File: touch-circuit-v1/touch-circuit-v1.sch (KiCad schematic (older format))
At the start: 11 parts, among them U1 Opamp_Dual_Generic

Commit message: add footprints
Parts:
- BT1: footprint (none) -> Battery:BatteryHolder_LINX_BAT-HLD-012-SMT
- C1: footprint (none) -> Capacitor_SMD:C_0805_2012Metric_Pad1.15x1.40mm_HandSolder
- D1: footprint (none) -> Diode_SMD:D_0805_2012Metric_Pad1.15x1.40mm_HandSolder
- D2: footprint (none) -> LED_SMD:LED_0805_2012Metric_Pad1.15x1.40mm_HandSolder
- R1, R2, R3, R4, R5, R6: footprint (none) -> Resistor_SMD:R_0805_2012Metric_Pad1.15x1.40mm_HandSolder
- U1: footprint (none) -> Package_SO:SO-8_5.3x6.2mm_P1.27mm
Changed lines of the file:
@@
 F 0 "U1" H 7050 4117 50  0000 C CNN
 F 1 "Opamp_Dual_Generic" H 7050 4026 50  0000 C CNN
-F 2 "" H 7050 3750 50  0001 C CNN
+F 2 "Package_SO:SO-8_5.3x6.2mm_P1.27mm" H 7050 3750 50  0001 C CNN
 F 3 "~" H 7050 3750 50  0001 C CNN
 	2    7050 3750
@@
 F 0 "U1" H 3008 3396 50  0000 L CNN
 F 1 "Opamp_Dual_Generic" H 3008 3305 50  0000 L CNN
-F 2 "" H 3050 3350 50  0001 C CNN
+F 2 "Package_SO:SO-8_5.3x6.2mm_P1.27mm" H 3050 3350 50  0001 C CNN
 F 3 "~" H 3050 3350 50  0001 C CNN
 	3    3050 3350
@@
 F 0 "U1" H 5200 3517 50  0000 C CNN
 F 1 "Opamp_Dual_Generic" H 5200 3426 50  0000 C CNN
-F 2 "" H 5200 3150 50  0001 C CNN
+F 2 "Package_SO:SO-8_5.3x6.2mm_P1.27mm" H 5200 3150 50  0001 C CNN
 F 3 "~" H 5200 3150 50  0001 C CNN
 	1    5200 3150
@@
 F 0 "D2" H 7892 3495 50  0000 C CNN
 F 1 "LED" H 7892 3586 50  0000 C CNN
-F 2 "" H 7900 3750 50  0001 C CNN
+F 2 "LED_SMD:LED_0805_2012Metric_Pad1.15x1.40mm_HandSolder" H 7900 3750 50  0001 C CNN
 F 3 "~" H 7900 3750 50  0001 C CNN
 	1    7900 3750
@@
 F 0 "R2" H 4518 2846 50  0000 L CNN
 F 1 "R_US" H 4518 2755 50  0000 L CNN
-F 2 "" V 4490 2790 50  0001 C CNN
+F 2 "Resistor_SMD:R_0805_2012Metric_Pad1.15x1.40mm_HandSolder" V 4490 2790 50  0001 C CNN
 F 3 "~" H 4450 2800 50  0001 C CNN
 	1    4450 2800
@@
 F 0 "C1" H 6415 3946 50  0000 L CNN
 F 1 "C" H 6415 3855 50  0000 L CNN
-F 2 "" H 6338 3750 50  0001 C CNN
+F 2 "Capacitor_SMD:C_0805_2012Metric_Pad1.15x1.40mm_HandSolder" H 6338 3750 50  0001 C CNN
 F 3 "~" H 6300 3900 50  0001 C CNN
 	1    6300 3900
@@
 F 0 "D1" H 6050 2934 50  0000 C CNN
 F 1 "D" H 6050 3025 50  0000 C CNN
-F 2 "" H 6050 3150 50  0001 C CNN
+F 2 "Diode_SMD:D_0805_2012Metric_Pad1.15x1.40mm_HandSolder" H 6050 3150 50  0001 C CNN
 F 3 "~" H 6050 3150 50  0001 C CNN
 	1    6050 3150
@@
 F 0 "R3" H 4518 3546 50  0000 L CNN
 F 1 "R_US" H 4518 3455 50  0000 L CNN
-F 2 "" V 4490 3490 50  0001 C CNN
+F 2 "Resistor_SMD:R_0805_2012Metric_Pad1.15x1.40mm_HandSolder" V 4490 3490 50  0001 C CNN
 F 3 "~" H 4450 3500 50  0001 C CNN
 	1    4450 3500
@@
 F 0 "R6" H 8218 4046 50  0000 L CNN
 F 1 "R_US" H 8218 3955 50  0000 L CNN
-F 2 "" V 8190 3990 50  0001 C CNN
+F 2 "Resistor_SMD:R_0805_2012Metric_Pad1.15x1.40mm_HandSolder" V 8190 3990 50  0001 C CNN
 F 3 "~" H 8150 4000 50  0001 C CNN
 	1    8150 4000
@@
 F 0 "R4" H 5868 3446 50  0000 L CNN
 F 1 "R_US" H 5868 3355 50  0000 L CNN
-F 2 "" V 5840 3390 50  0001 C CNN
+F 2 "Resistor_SMD:R_0805_2012Metric_Pad1.15x1.40mm_HandSolder" V 5840 3390 50  0001 C CNN
 F 3 "~" H 5800 3400 50  0001 C CNN
 	1    5800 3400
@@
 F 0 "R5" H 6368 3446 50  0000 L CNN
 F 1 "R_US" H 6368 3355 50  0000 L CNN
-F 2 "" V 6340 3390 50  0001 C CNN
+F 2 "Resistor_SMD:R_0805_2012Metric_Pad1.15x1.40mm_HandSolder" V 6340 3390 50  0001 C CNN
 F 3 "~" H 6300 3400 50  0001 C CNN
 	1    6300 3400
@@
 F 0 "R1" H 4068 3546 50  0000 L CNN
 F 1 "R_US" H 4068 3455 50  0000 L CNN
-F 2 "" V 4040 3490 50  0001 C CNN
+F 2 "Resistor_SMD:R_0805_2012Metric_Pad1.15x1.40mm_HandSolder" V 4040 3490 50  0001 C CNN
 F 3 "~" H 4000 3500 50  0001 C CNN
 	1    4000 3500
@@
 F 0 "BT1" H 2268 3496 50  0000 L CNN
 F 1 "Battery_Cell" H 2268 3405 50  0000 L CNN
-F 2 "" V 2150 3460 50  0001 C CNN
+F 2 "Battery:BatteryHolder_LINX_BAT-HLD-012-SMT" V 2150 3460 50  0001 C CNN
 F 3 "~" V 2150 3460 50  0001 C CNN
 	1    2150 3400

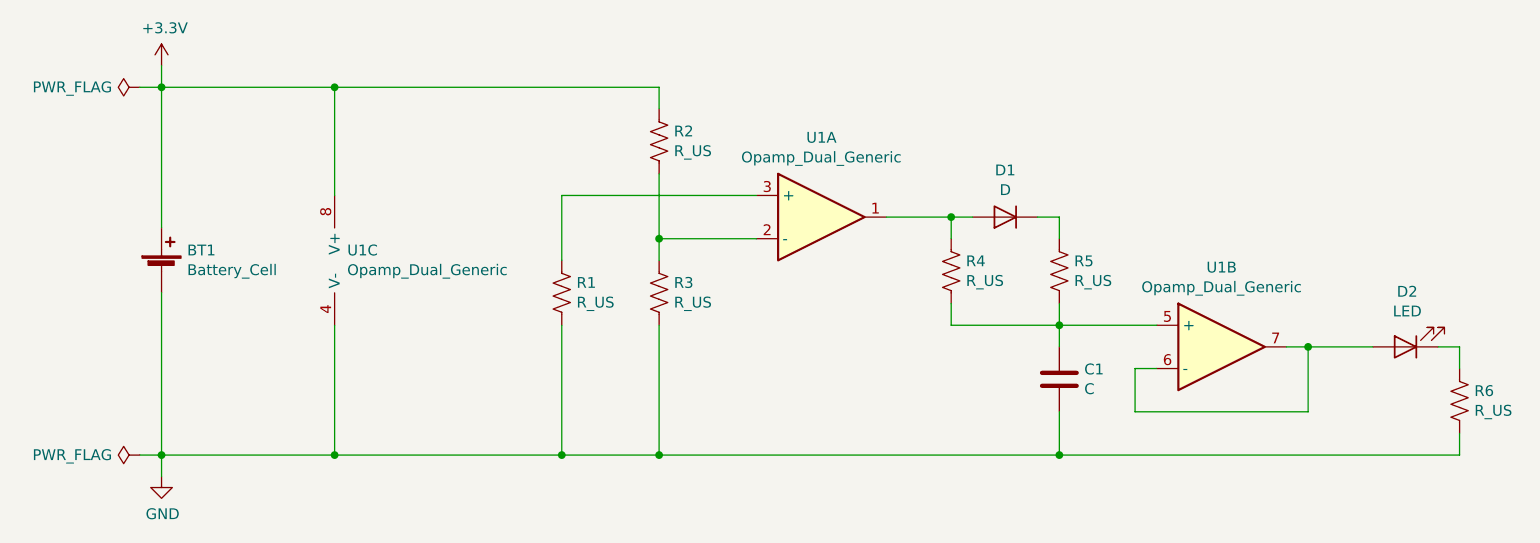
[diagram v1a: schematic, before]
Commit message: add mounting holes
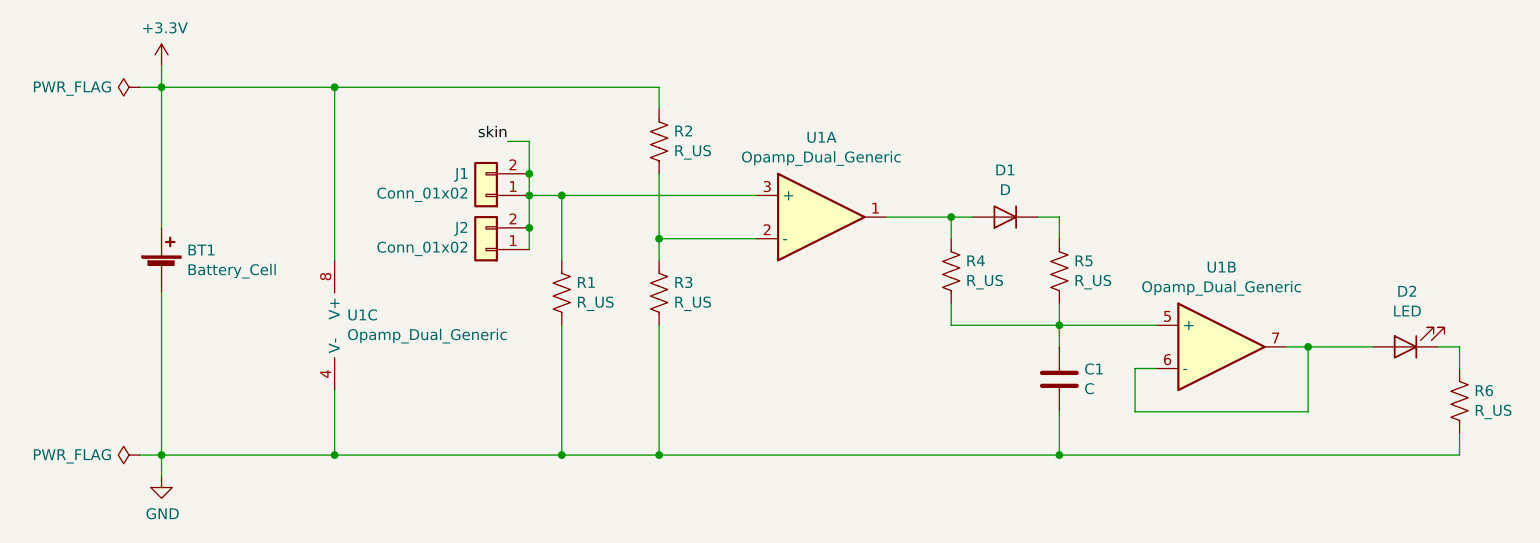
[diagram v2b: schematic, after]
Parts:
- added J1, J2: Conn_01x02, Connector_PinHeader_2.54mm:PinHeader_1x02_P2.54mm_Vertical, symbol Connector_Generic:Conn_01x02
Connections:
- net skin: now reaches R1.1, U1.3 (+)
- net skin: now also J1.1 (Pin_1), J1.2 (Pin_2), J2.1 (Pin_1), J2.2 (Pin_2)
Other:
- moved on the sheet: U1C
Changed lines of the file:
@@
 EESchema Schematic File Version 4
+LIBS:touch-circuit-v1-cache
 EELAYER 26 0
 EELAYER END
@@
 L Device:Opamp_Dual_Generic U1
 U 3 1 5E3073DB
-P 3050 3350
-F 0 "U1" H 3008 3396 50  0000 L CNN
-F 1 "Opamp_Dual_Generic" H 3008 3305 50  0000 L CNN
-F 2 "Package_SO:SO-8_5.3x6.2mm_P1.27mm" H 3050 3350 50  0001 C CNN
-F 3 "~" H 3050 3350 50  0001 C CNN
-	3    3050 3350
+P 3050 3650
+F 0 "U1" H 3008 3696 50  0000 L CNN
+F 1 "Opamp_Dual_Generic" H 3008 3605 50  0000 L CNN
+F 2 "Package_SO:SO-8_5.3x6.2mm_P1.27mm" H 3050 3650 50  0001 C CNN
+F 3 "~" H 3050 3650 50  0001 C CNN
+	3    3050 3650
 	1    0    0    -1
 $EndComp
@@
 Connection ~ 4450 3250
 Wire Wire Line
-	4900 3050 4000 3050
-Wire Wire Line
-	4000 3050 4000 3350
-Wire Wire Line
 	5800 3550 5800 3650
 Wire Wire Line
@@
 Connection ~ 5800 3150
 Wire Wire Line
-	2950 2550 2950 3050
-Wire Wire Line
-	2950 3650 2950 4250
+	2950 2550 2950 3350
+Wire Wire Line
+	2950 3950 2950 4250
 Wire Wire Line
 	2950 4250 4000 4250
@@
 Wire Wire Line
 	2050 4250 2150 4250
+Text Label 3750 2800 2    50   ~ 0
+skin
+$Comp
+L Connector_Generic:Conn_01x02 J1
+U 1 1 5E30C6B3
+P 3650 3050
+F 0 "J1" H 3730 2950 50  0000 L CNN
+F 1 "Conn_01x02" H 3730 3041 50  0000 L CNN
+F 2 "Connector_PinHeader_2.54mm:PinHeader_1x02_P2.54mm_Vertical" H 3650 3050 50  0001 C CNN
+F 3 "~" H 3650 3050 50  0001 C CNN
+	1    3650 3050
+	-1   0    0    1
+$EndComp
+$Comp
+L Connector_Generic:Conn_01x02 J2
+U 1 1 5E312800
+P 3650 3300
+F 0 "J2" H 3730 3200 50  0000 L CNN
+F 1 "Conn_01x02" H 3730 3291 50  0000 L CNN
+F 2 "Connector_PinHeader_2.54mm:PinHeader_1x02_P2.54mm_Vertical" H 3650 3300 50  0001 C CNN
+F 3 "~" H 3650 3300 50  0001 C CNN
+	1    3650 3300
+	-1   0    0    1
+$EndComp
+Wire Wire Line
+	4900 3050 4000 3050
+Wire Wire Line
+	4000 3050 4000 3350
+Connection ~ 3850 3050
+Wire Wire Line
+	3850 3050 3850 2950
+Connection ~ 3850 3200
+Wire Wire Line
+	3850 3200 3850 3050
+Wire Wire Line
+	3850 3200 3850 3300
+Wire Wire Line
+	3750 2800 3850 2800
+Wire Wire Line
+	3850 2800 3850 2950
+Connection ~ 3850 2950
+Wire Wire Line
+	3850 3050 4000 3050
+Connection ~ 4000 3050
 $EndSCHEMATC

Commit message: add silk and update mounting footprints
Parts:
- J1, J2: footprint Connector_PinHeader_2.54mm:PinHeader_1x02_P2.54mm_Vertical -> touch-circuit-v1:PinHeader_1x02_P2.54mm_Vertical_nosilk
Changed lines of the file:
@@
 F 0 "J1" H 3730 2950 50  0000 L CNN
 F 1 "Conn_01x02" H 3730 3041 50  0000 L CNN
-F 2 "Connector_PinHeader_2.54mm:PinHeader_1x02_P2.54mm_Vertical" H 3650 3050 50  0001 C CNN
+F 2 "touch-circuit-v1:PinHeader_1x02_P2.54mm_Vertical_nosilk" H 3650 3050 50  0001 C CNN
 F 3 "~" H 3650 3050 50  0001 C CNN
 	1    3650 3050
@@
 F 0 "J2" H 3730 3200 50  0000 L CNN
 F 1 "Conn_01x02" H 3730 3291 50  0000 L CNN
-F 2 "Connector_PinHeader_2.54mm:PinHeader_1x02_P2.54mm_Vertical" H 3650 3300 50  0001 C CNN
+F 2 "touch-circuit-v1:PinHeader_1x02_P2.54mm_Vertical_nosilk" H 3650 3300 50  0001 C CNN
 F 3 "~" H 3650 3300 50  0001 C CNN
 	1    3650 3300

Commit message: change the opamp module I'm using
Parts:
- BT1: value Battery_Cell -> CR1220; Link (none) -> https://www.mouser.com/ProductDetail/BAT-HLD-012-SMT
- C1: value C -> 10u; Link (none) -> https://www.mouser.com/ProductDetail/CGA4J1X7R0J106K125AC
- D1: Link (none) -> https://www.mouser.com/ProductDetail/SD0805S040S0R5
- D2: Link (none) -> https://www.mouser.com/ProductDetail/FKY1112H-TR
- J1, J2: value Conn_01x02 -> Loop
- R1, R2: value R_US -> 3.3M
- R3: value R_US -> 500k
- R4: value R_US -> 100k
- R5: value R_US -> 330k
- R6: value R_US -> 68
- U1: value Opamp_Dual_Generic -> LM358PSR; Link (none) -> https://www.mouser.com/ProductDetail/LM358PSR
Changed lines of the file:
@@
 P 7050 3750
 F 0 "U1" H 7050 4117 50  0000 C CNN
-F 1 "Opamp_Dual_Generic" H 7050 4026 50  0000 C CNN
+F 1 "LM358PSR" H 7050 4026 50  0000 C CNN
 F 2 "Package_SO:SO-8_5.3x6.2mm_P1.27mm" H 7050 3750 50  0001 C CNN
-F 3 "~" H 7050 3750 50  0001 C CNN
+F 3 "https://www.ti.com/lit/ds/symlink/lm358.pdf" H 7050 3750 50  0001 C CNN
+F 4 "https://www.mouser.com/ProductDetail/LM358PSR" H 0   0   50  0001 C CNN "Link"
 	2    7050 3750
 	1    0    0    -1
@@
 P 3050 3650
 F 0 "U1" H 3008 3696 50  0000 L CNN
-F 1 "Opamp_Dual_Generic" H 3008 3605 50  0000 L CNN
+F 1 "LM358PSR" H 3008 3605 50  0000 L CNN
 F 2 "Package_SO:SO-8_5.3x6.2mm_P1.27mm" H 3050 3650 50  0001 C CNN
-F 3 "~" H 3050 3650 50  0001 C CNN
+F 3 "https://www.ti.com/lit/ds/symlink/lm358.pdf" H 3050 3650 50  0001 C CNN
+F 4 "https://www.mouser.com/ProductDetail/LM358PSR" H 0   0   50  0001 C CNN "Link"
 	3    3050 3650
 	1    0    0    -1
@@
 P 5200 3150
 F 0 "U1" H 5200 3517 50  0000 C CNN
-F 1 "Opamp_Dual_Generic" H 5200 3426 50  0000 C CNN
+F 1 "LM358PSR" H 5200 3426 50  0000 C CNN
 F 2 "Package_SO:SO-8_5.3x6.2mm_P1.27mm" H 5200 3150 50  0001 C CNN
-F 3 "~" H 5200 3150 50  0001 C CNN
+F 3 "https://www.ti.com/lit/ds/symlink/lm358.pdf" H 5200 3150 50  0001 C CNN
+F 4 "https://www.mouser.com/ProductDetail/LM358PSR" H 5200 3150 50  0001 C CNN "Link"
 	1    5200 3150
 	1    0    0    -1
@@
 F 1 "LED" H 7892 3586 50  0000 C CNN
 F 2 "LED_SMD:LED_0805_2012Metric_Pad1.15x1.40mm_HandSolder" H 7900 3750 50  0001 C CNN
-F 3 "~" H 7900 3750 50  0001 C CNN
+F 3 "http://www.stanley-components.com/php/downloaddatafile.php?rp=0,FKY1112H-TR_e.pdf" H 7900 3750 50  0001 C CNN
+F 4 "https://www.mouser.com/ProductDetail/FKY1112H-TR" H 0   0   50  0001 C CNN "Link"
 	1    7900 3750
 	-1   0    0    1
@@
 P 4450 2800
 F 0 "R2" H 4518 2846 50  0000 L CNN
-F 1 "R_US" H 4518 2755 50  0000 L CNN
+F 1 "3.3M" H 4518 2755 50  0000 L CNN
 F 2 "Resistor_SMD:R_0805_2012Metric_Pad1.15x1.40mm_HandSolder" V 4490 2790 50  0001 C CNN
 F 3 "~" H 4450 2800 50  0001 C CNN
@@
 P 6300 3900
 F 0 "C1" H 6415 3946 50  0000 L CNN
-F 1 "C" H 6415 3855 50  0000 L CNN
+F 1 "10u" H 6415 3855 50  0000 L CNN
 F 2 "Capacitor_SMD:C_0805_2012Metric_Pad1.15x1.40mm_HandSolder" H 6338 3750 50  0001 C CNN
-F 3 "~" H 6300 3900 50  0001 C CNN
+F 3 "https://product.tdk.com/en/search/capacitor/ceramic/mlcc/info?part_no=CGA4J1X7R0J106K125AC" H 6300 3900 50  0001 C CNN
+F 4 "https://www.mouser.com/ProductDetail/CGA4J1X7R0J106K125AC" H 0   0   50  0001 C CNN "Link"
 	1    6300 3900
 	1    0    0    -1
@@
 F 1 "D" H 6050 3025 50  0000 C CNN
 F 2 "Diode_SMD:D_0805_2012Metric_Pad1.15x1.40mm_HandSolder" H 6050 3150 50  0001 C CNN
-F 3 "~" H 6050 3150 50  0001 C CNN
+F 3 "http://datasheets.avx.com/schottky.pdf" H 6050 3150 50  0001 C CNN
+F 4 "https://www.mouser.com/ProductDetail/SD0805S040S0R5" H 0   0   50  0001 C CNN "Link"
 	1    6050 3150
 	-1   0    0    1
@@
 P 4450 3500
 F 0 "R3" H 4518 3546 50  0000 L CNN
-F 1 "R_US" H 4518 3455 50  0000 L CNN
+F 1 "500k" H 4518 3455 50  0000 L CNN
 F 2 "Resistor_SMD:R_0805_2012Metric_Pad1.15x1.40mm_HandSolder" V 4490 3490 50  0001 C CNN
 F 3 "~" H 4450 3500 50  0001 C CNN
@@
 P 8150 4000
 F 0 "R6" H 8218 4046 50  0000 L CNN
-F 1 "R_US" H 8218 3955 50  0000 L CNN
+F 1 "68" H 8218 3955 50  0000 L CNN
 F 2 "Resistor_SMD:R_0805_2012Metric_Pad1.15x1.40mm_HandSolder" V 8190 3990 50  0001 C CNN
 F 3 "~" H 8150 4000 50  0001 C CNN
@@
 P 5800 3400
 F 0 "R4" H 5868 3446 50  0000 L CNN
-F 1 "R_US" H 5868 3355 50  0000 L CNN
+F 1 "100k" H 5868 3355 50  0000 L CNN
 F 2 "Resistor_SMD:R_0805_2012Metric_Pad1.15x1.40mm_HandSolder" V 5840 3390 50  0001 C CNN
 F 3 "~" H 5800 3400 50  0001 C CNN
@@
 P 6300 3400
 F 0 "R5" H 6368 3446 50  0000 L CNN
-F 1 "R_US" H 6368 3355 50  0000 L CNN
+F 1 "330k" H 6368 3355 50  0000 L CNN
 F 2 "Resistor_SMD:R_0805_2012Metric_Pad1.15x1.40mm_HandSolder" V 6340 3390 50  0001 C CNN
 F 3 "~" H 6300 3400 50  0001 C CNN
@@
 P 4000 3500
 F 0 "R1" H 4068 3546 50  0000 L CNN
-F 1 "R_US" H 4068 3455 50  0000 L CNN
+F 1 "3.3M" H 4068 3455 50  0000 L CNN
 F 2 "Resistor_SMD:R_0805_2012Metric_Pad1.15x1.40mm_HandSolder" V 4040 3490 50  0001 C CNN
 F 3 "~" H 4000 3500 50  0001 C CNN
@@
 P 2150 3400
 F 0 "BT1" H 2268 3496 50  0000 L CNN
-F 1 "Battery_Cell" H 2268 3405 50  0000 L CNN
+F 1 "CR1220" H 2268 3405 50  0000 L CNN
 F 2 "Battery:BatteryHolder_LINX_BAT-HLD-012-SMT" V 2150 3460 50  0001 C CNN
-F 3 "~" V 2150 3460 50  0001 C CNN
+F 3 "https://linxtechnologies.com/wp/wp-content/uploads/bat-hld-012-smt.pdf" V 2150 3460 50  0001 C CNN
+F 4 "https://www.mouser.com/ProductDetail/BAT-HLD-012-SMT" H 0   0   50  0001 C CNN "Link"
 	1    2150 3400
 	1    0    0    -1
@@
 P 3650 3050
 F 0 "J1" H 3730 2950 50  0000 L CNN
-F 1 "Conn_01x02" H 3730 3041 50  0000 L CNN
+F 1 "Loop" H 3730 3041 50  0000 L CNN
 F 2 "touch-circuit-v1:PinHeader_1x02_P2.54mm_Vertical_nosilk" H 3650 3050 50  0001 C CNN
 F 3 "~" H 3650 3050 50  0001 C CNN
@@
 P 3650 3300
 F 0 "J2" H 3730 3200 50  0000 L CNN
-F 1 "Conn_01x02" H 3730 3291 50  0000 L CNN
+F 1 "Loop" H 3730 3291 50  0000 L CNN
 F 2 "touch-circuit-v1:PinHeader_1x02_P2.54mm_Vertical_nosilk" H 3650 3300 50  0001 C CNN
 F 3 "~" H 3650 3300 50  0001 C CNN
